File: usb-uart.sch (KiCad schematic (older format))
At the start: 11 parts, among them P5 USB-C-2.0-FEMALE, U3 CH340C

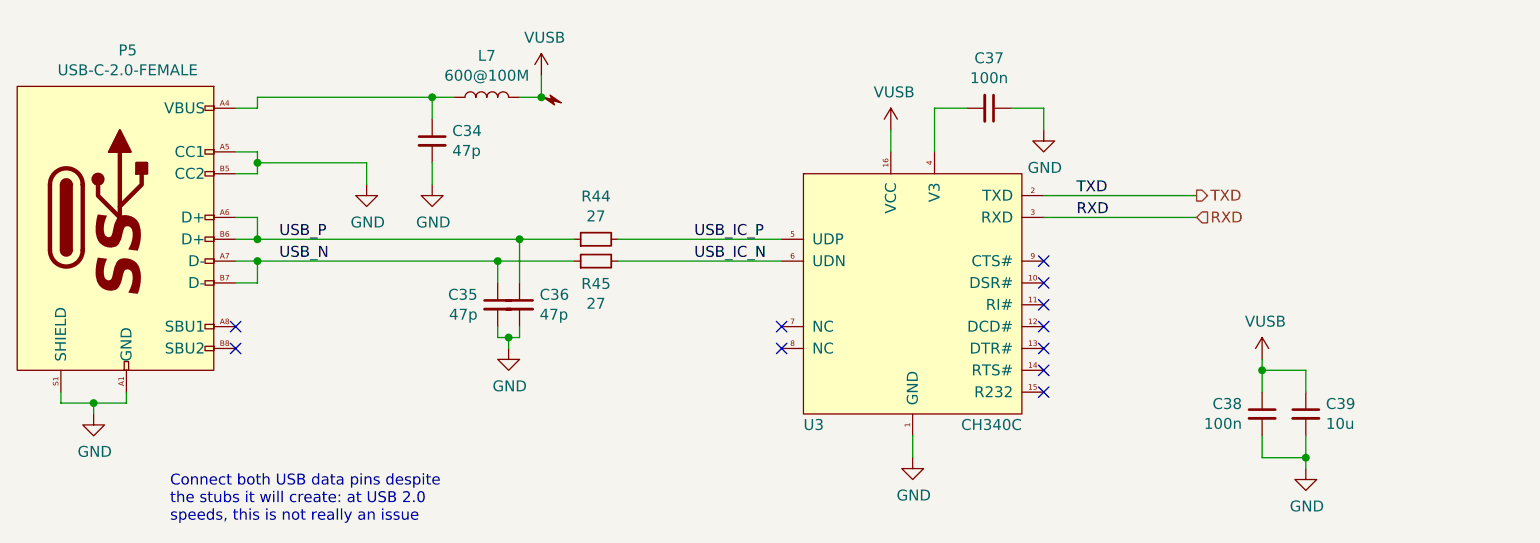
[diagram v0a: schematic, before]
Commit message: sch, pcb: Add testpads on lots of signals
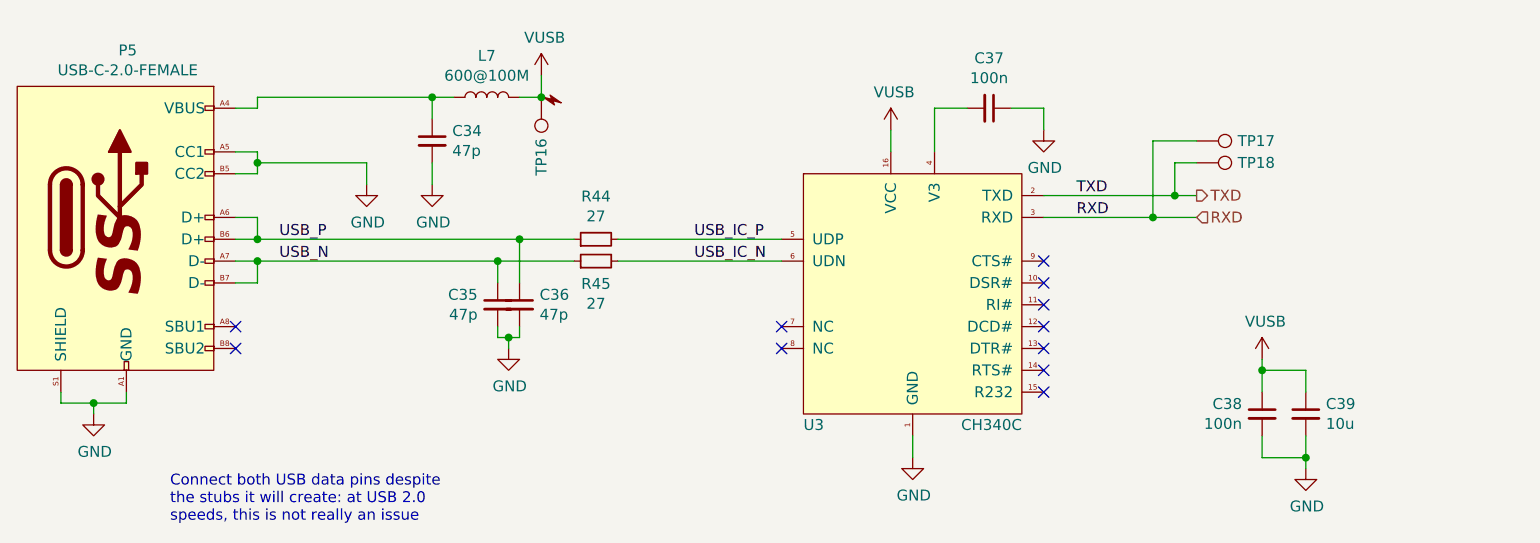
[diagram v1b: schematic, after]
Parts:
- added TP16, TP17, TP18: TestPoint, TestPoint:TestPoint_Pad_D1.0mm, symbol Connector:TestPoint
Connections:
- net RXD: now also TP17.1
- net TXD: now also TP18.1
- net VUSB: now also TP16.1
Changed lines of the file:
@@
 Connection ~ 8700 4800
 Wire Wire Line
-	7500 3600 8200 3600
-Wire Wire Line
-	8200 3700 7500 3700
+	7500 3600 8100 3600
+Wire Wire Line
+	8200 3700 8000 3700
 Text Label 7650 3600 0    50   ~ 0
 TXD
@@
 $EndComp
 Connection ~ 5200 3150
+$Comp
+L Connector:TestPoint TP?
+U 1 1 5D3F5908
+P 8200 3450
+AR Path="/5D05A5E1/5D3F5908" Ref="TP?"  Part="1"
+AR Path="/5CE77C37/5D3F5908" Ref="TP?"  Part="1"
+AR Path="/5D2774DB/5D3F5908" Ref="TP18"  Part="1"
+F 0 "TP18" V 8200 3638 50  0000 L CNN
+F 1 "TestPoint" V 8245 3638 50  0001 L CNN
+F 2 "TestPoint:TestPoint_Pad_D1.0mm" H 8400 3450 50  0001 C CNN
+F 3 "~" H 8400 3450 50  0001 C CNN
+	1    8200 3450
+	0    1    1    0
+$EndComp
+$Comp
+L Connector:TestPoint TP?
+U 1 1 5D3F64DD
+P 8200 3350
+AR Path="/5D05A5E1/5D3F64DD" Ref="TP?"  Part="1"
+AR Path="/5CE77C37/5D3F64DD" Ref="TP?"  Part="1"
+AR Path="/5D2774DB/5D3F64DD" Ref="TP17"  Part="1"
+F 0 "TP17" V 8200 3538 50  0000 L CNN
+F 1 "TestPoint" V 8245 3538 50  0001 L CNN
+F 2 "TestPoint:TestPoint_Pad_D1.0mm" H 8400 3350 50  0001 C CNN
+F 3 "~" H 8400 3350 50  0001 C CNN
+	1    8200 3350
+	0    1    1    0
+$EndComp
+Wire Wire Line
+	8200 3450 8100 3450
+Wire Wire Line
+	8100 3450 8100 3600
+Connection ~ 8100 3600
+Wire Wire Line
+	8100 3600 8200 3600
+Wire Wire Line
+	8200 3350 8000 3350
+Wire Wire Line
+	8000 3350 8000 3700
+Connection ~ 8000 3700
+Wire Wire Line
+	8000 3700 7500 3700
+$Comp
+L Connector:TestPoint TP?
+U 1 1 5D3F8607
+P 5200 3150
+AR Path="/5D05A5E1/5D3F8607" Ref="TP?"  Part="1"
+AR Path="/5CE77C37/5D3F8607" Ref="TP?"  Part="1"
+AR Path="/5D2774DB/5D3F8607" Ref="TP16"  Part="1"
+F 0 "TP16" V 5200 3338 50  0000 L CNN
+F 1 "TestPoint" V 5245 3338 50  0001 L CNN
+F 2 "TestPoint:TestPoint_Pad_D1.0mm" H 5400 3150 50  0001 C CNN
+F 3 "~" H 5400 3150 50  0001 C CNN
+	1    5200 3150
+	-1   0    0    1
+$EndComp
 $EndSCHEMATC

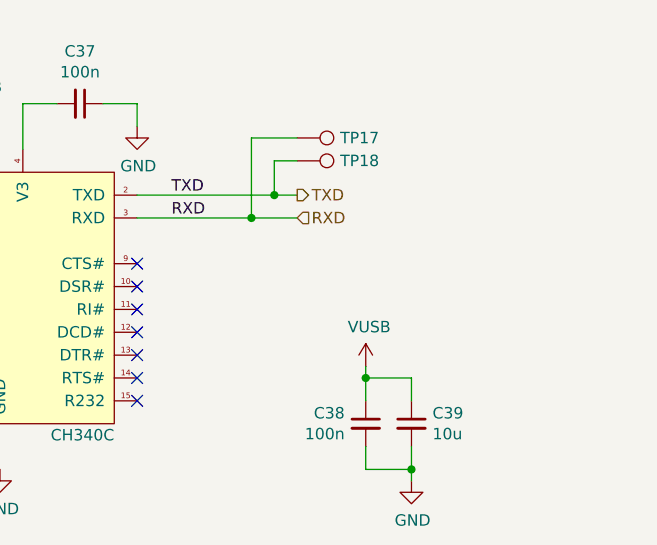
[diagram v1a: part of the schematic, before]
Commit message: sch, pcb: Connect ISL8033 PGND to GND, fix UART
Pimouss won't boot when its TXD line is pulled up, which the CH340 does.
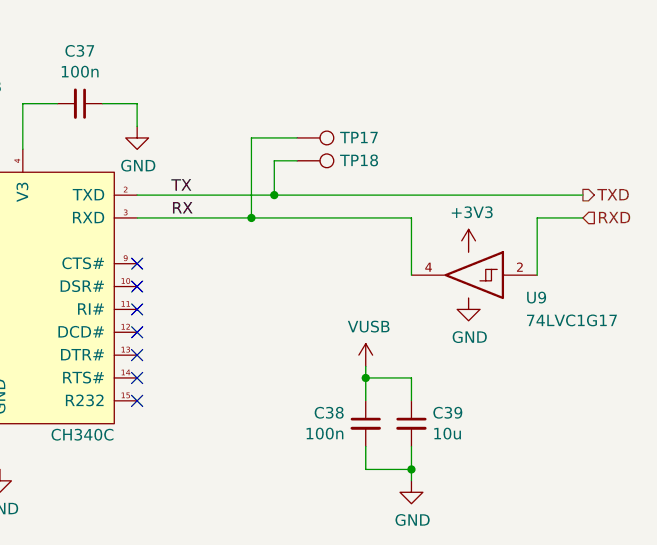
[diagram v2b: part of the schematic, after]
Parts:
- added U9: 74LVC1G17, Package_TO_SOT_SMD:SOT-23-5, symbol 74xGxx:74LVC1G17
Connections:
- net GND: now also U9.3 (GND)
- net RXD: now also U9.2; no longer TP17.1, U3.3 (RXD)
- new net +3V3: U9.5 (VCC)
- new net RX: TP17.1, U3.3 (RXD), U9.4
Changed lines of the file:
@@
 Wire Wire Line
 	7500 3600 8100 3600
-Wire Wire Line
-	8200 3700 8000 3700
 Text Label 7650 3600 0    50   ~ 0
-TXD
+TX
 Text Label 7650 3700 0    50   ~ 0
-RXD
+RX
 Wire Wire Line
 	3900 3450 4400 3450
@@
 	1    0    0    -1
 $EndComp
-Text HLabel 8200 3600 2    50   Output ~ 0
+Text HLabel 9450 3600 2    50   Output ~ 0
 TXD
-Text HLabel 8200 3700 2    50   Input ~ 0
+Text HLabel 9450 3700 2    50   Input ~ 0
 RXD
 $Comp
@@
 	8100 3450 8100 3600
 Connection ~ 8100 3600
-Wire Wire Line
-	8100 3600 8200 3600
 Wire Wire Line
 	8200 3350 8000 3350
@@
 	-1   0    0    1
 $EndComp
+Wire Wire Line
+	8700 3700 8700 3950
+Wire Wire Line
+	9250 3950 9250 3700
+Wire Wire Line
+	9250 3700 9450 3700
+Wire Wire Line
+	8000 3700 8700 3700
+$Comp
+L power:+3V3 #PWR?
+U 1 1 5D6A370C
+P 8950 3850
+AR Path="/5D0A0558/5D6A370C" Ref="#PWR?"  Part="1"
+AR Path="/5D2774DB/5D6A370C" Ref="#PWR0160"  Part="1"
+F 0 "#PWR0160" H 8950 3700 50  0001 C CNN
+F 1 "+3V3" H 8965 4023 50  0000 C CNN
+F 2 "" H 8950 3850 50  0001 C CNN
+F 3 "" H 8950 3850 50  0001 C CNN
+	1    8950 3850
+	1    0    0    -1
+$EndComp
+$Comp
+L power:GND #PWR0195
+U 1 1 5D6A4790
+P 8950 4050
+F 0 "#PWR0195" H 8950 3800 50  0001 C CNN
+F 1 "GND" H 8955 3877 50  0000 C CNN
+F 2 "" H 8950 4050 50  0001 C CNN
+F 3 "" H 8950 4050 50  0001 C CNN
+	1    8950 4050
+	1    0    0    -1
+$EndComp
+Wire Wire Line
+	8100 3600 9450 3600
+$Comp
+L 74xGxx:74LVC1G17 U9
+U 1 1 5D6876B8
+P 8950 3950
+F 0 "U9" H 8700 3850 50  0000 R CNN
+F 1 "74LVC1G17" H 8700 3750 50  0000 R CNN
+F 2 "Package_TO_SOT_SMD:SOT-23-5" H 8950 3950 50  0001 C CNN
+F 3 "http://www.ti.com/lit/sg/scyt129e/scyt129e.pdf" H 8950 3950 50  0001 C CNN
+	1    8950 3950
+	-1   0    0    -1
+$EndComp
 $EndSCHEMATC

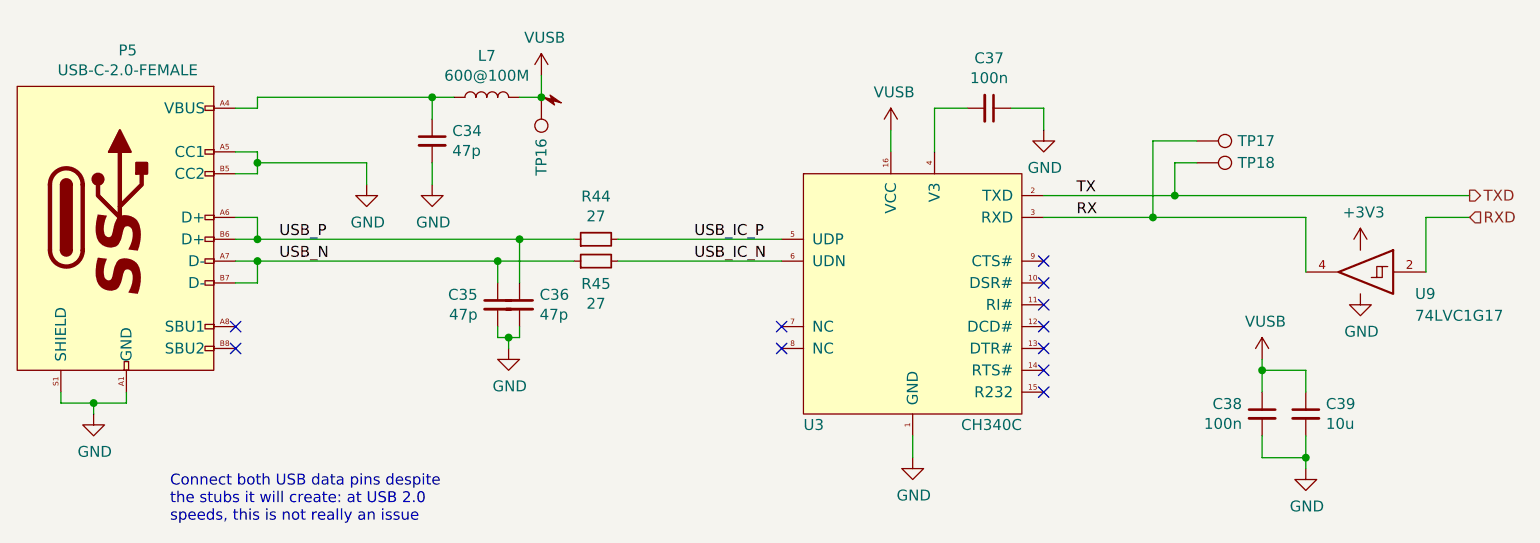
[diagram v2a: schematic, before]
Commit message: sch: Replace CH340C with FT230XS
CH340 pulls up its RXD line, which makes the pimouss unhappy: nothing
will get out of the UART port when its TXD line is held high on boot
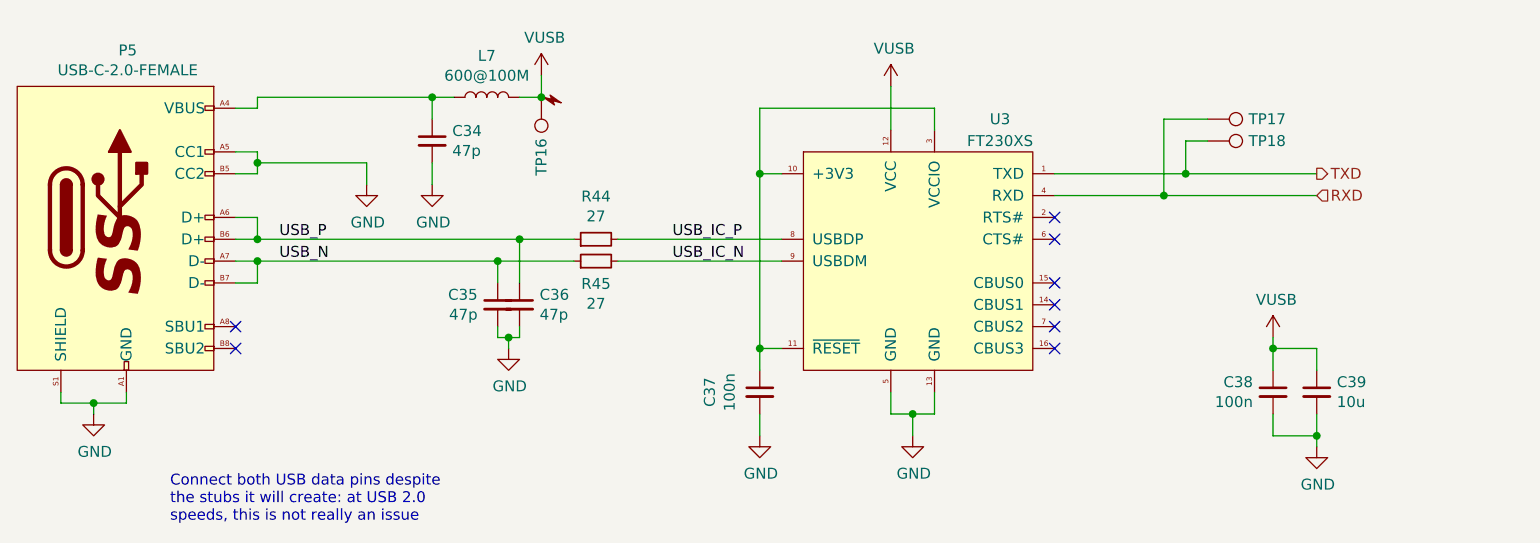
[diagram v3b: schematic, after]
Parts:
- removed U3: CH340C, Package_SO:SOIC-16_3.9x9.9mm_P1.27mm, symbol pimouss-motherboard:CH340C
- removed U9: 74LVC1G17, Package_TO_SOT_SMD:SOT-23-5, symbol 74xGxx:74LVC1G17
- added U3: FT230XS, Package_SO:SSOP-16_3.9x4.9mm_P0.635mm, symbol pimouss-motherboard:FT230XS
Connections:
- net RX is gone; now on net RXD: TP17.1
- net GND: now also C37.2, U3.13 (GND), U3.5 (GND); no longer C37.1
- net RXD: now also U3.4 (RXD)
- net TXD: now also U3.1 (TXD)
- net USB_IC_N: now also U3.9 (USBDM)
- net USB_IC_P: now also U3.8 (USBDP)
- net VUSB: now also U3.12 (VCC)
- new net: C37.1, U3.10 (+3V3), U3.11 (~RESET), U3.3 (VCCIO)
- no-connect marks 11 -> 8
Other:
- moved on the sheet: C37, C38, C39, TP17, TP18

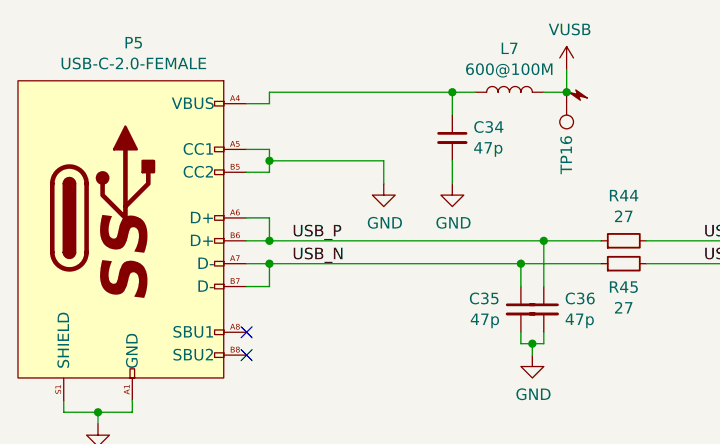
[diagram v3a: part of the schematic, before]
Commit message: sch, pcb: Replace CH340 with FT230 and add USB host port
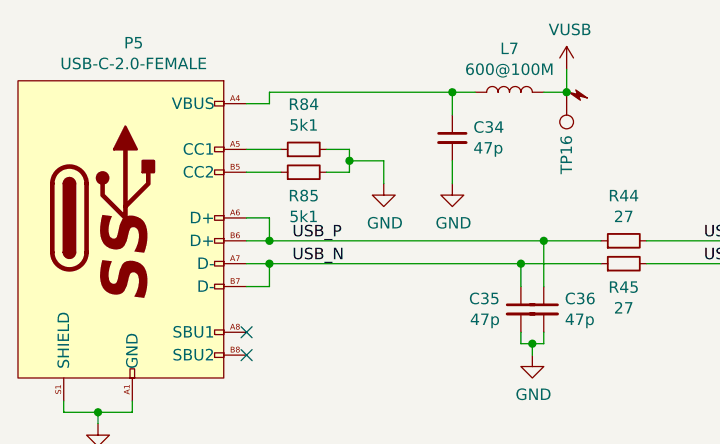
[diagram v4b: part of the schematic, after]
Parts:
- added R84, R85: 5k1, Resistor_SMD:R_0603_1608Metric, symbol Device:R_Small
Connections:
- net GND: now also R84.2, R85.2; no longer P5.A5 (CC1), P5.B5 (CC2)
- new net: P5.A5 (CC1), R84.1
- new net: P5.B5 (CC2), R85.1
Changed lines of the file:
@@
 Text Label 5800 3900 0    50   ~ 0
 USB_IC_N
-Text Label 4000 3800 0    50   ~ 0
-USB_P
 Text Label 4000 3900 0    50   ~ 0
 USB_N
@@
 Wire Wire Line
 	3000 4550 3000 4500
-Wire Wire Line
-	3800 3400 3900 3400
-Wire Wire Line
-	3900 3400 3900 3450
-Wire Wire Line
-	3800 3500 3900 3500
-Wire Wire Line
-	3900 3500 3900 3450
-Connection ~ 3900 3450
-$Comp
-L power:GND #PWR081
-U 1 1 5D280DF4
-P 4400 3550
-F 0 "#PWR081" H 4400 3300 50  0001 C CNN
-F 1 "GND" H 4405 3377 50  0000 C CNN
-F 2 "" H 4400 3550 50  0001 C CNN
-F 3 "" H 4400 3550 50  0001 C CNN
-	1    4400 3550
-	1    0    0    -1
-$EndComp
-Wire Wire Line
-	4400 3450 4400 3550
 $Comp
 L Device:L L?
@@
 	7550 3500 8150 3500
 Wire Wire Line
-	3900 3450 4400 3450
-Wire Wire Line
 	3000 4550 3150 4550
 $Comp
@@
 NoConn ~ 7550 4200
 NoConn ~ 7550 4300
+$Comp
+L Device:R_Small R84
+U 1 1 5DFFAFC5
+P 4050 3400
+F 0 "R84" V 4246 3400 50  0000 C CNN
+F 1 "5k1" V 4155 3400 50  0000 C CNN
+F 2 "Resistor_SMD:R_0603_1608Metric" H 4050 3400 50  0001 C CNN
+F 3 "~" H 4050 3400 50  0001 C CNN
+	1    4050 3400
+	0    -1   -1   0
+$EndComp
+$Comp
+L Device:R_Small R85
+U 1 1 5DFFAFCB
+P 4050 3500
+F 0 "R85" V 3946 3500 50  0000 C CNN
+F 1 "5k1" V 3855 3500 50  0000 C CNN
+F 2 "Resistor_SMD:R_0603_1608Metric" H 4050 3500 50  0001 C CNN
+F 3 "~" H 4050 3500 50  0001 C CNN
+	1    4050 3500
+	0    -1   -1   0
+$EndComp
+Wire Wire Line
+	3800 3400 3950 3400
+Wire Wire Line
+	3800 3500 3950 3500
+Wire Wire Line
+	4150 3400 4250 3400
+Wire Wire Line
+	4250 3400 4250 3450
+Wire Wire Line
+	4250 3500 4150 3500
+Connection ~ 4250 3450
+Wire Wire Line
+	4250 3450 4250 3500
+Text Label 4000 3800 0    50   ~ 0
+USB_P
+Wire Wire Line
+	4250 3450 4400 3450
+Wire Wire Line
+	4400 3450 4400 3550
+$Comp
+L power:GND #PWR081
+U 1 1 5D280DF4
+P 4400 3550
+F 0 "#PWR081" H 4400 3300 50  0001 C CNN
+F 1 "GND" H 4405 3377 50  0000 C CNN
+F 2 "" H 4400 3550 50  0001 C CNN
+F 3 "" H 4400 3550 50  0001 C CNN
+	1    4400 3550
+	1    0    0    -1
+$EndComp
 $EndSCHEMATC
